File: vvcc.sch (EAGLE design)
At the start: 52 parts, among them IC1 MCP40D19T-5K, IC2 RP2040, IC3 NCP1117LPST33T3G, IC4 16MB_Flash, IC5 LD117ADT-TR, IC6 CLXC8T245QRHLRQ1, J1 Micro-B, J2 302-S301, J3 302-S301, Q1 12MHz

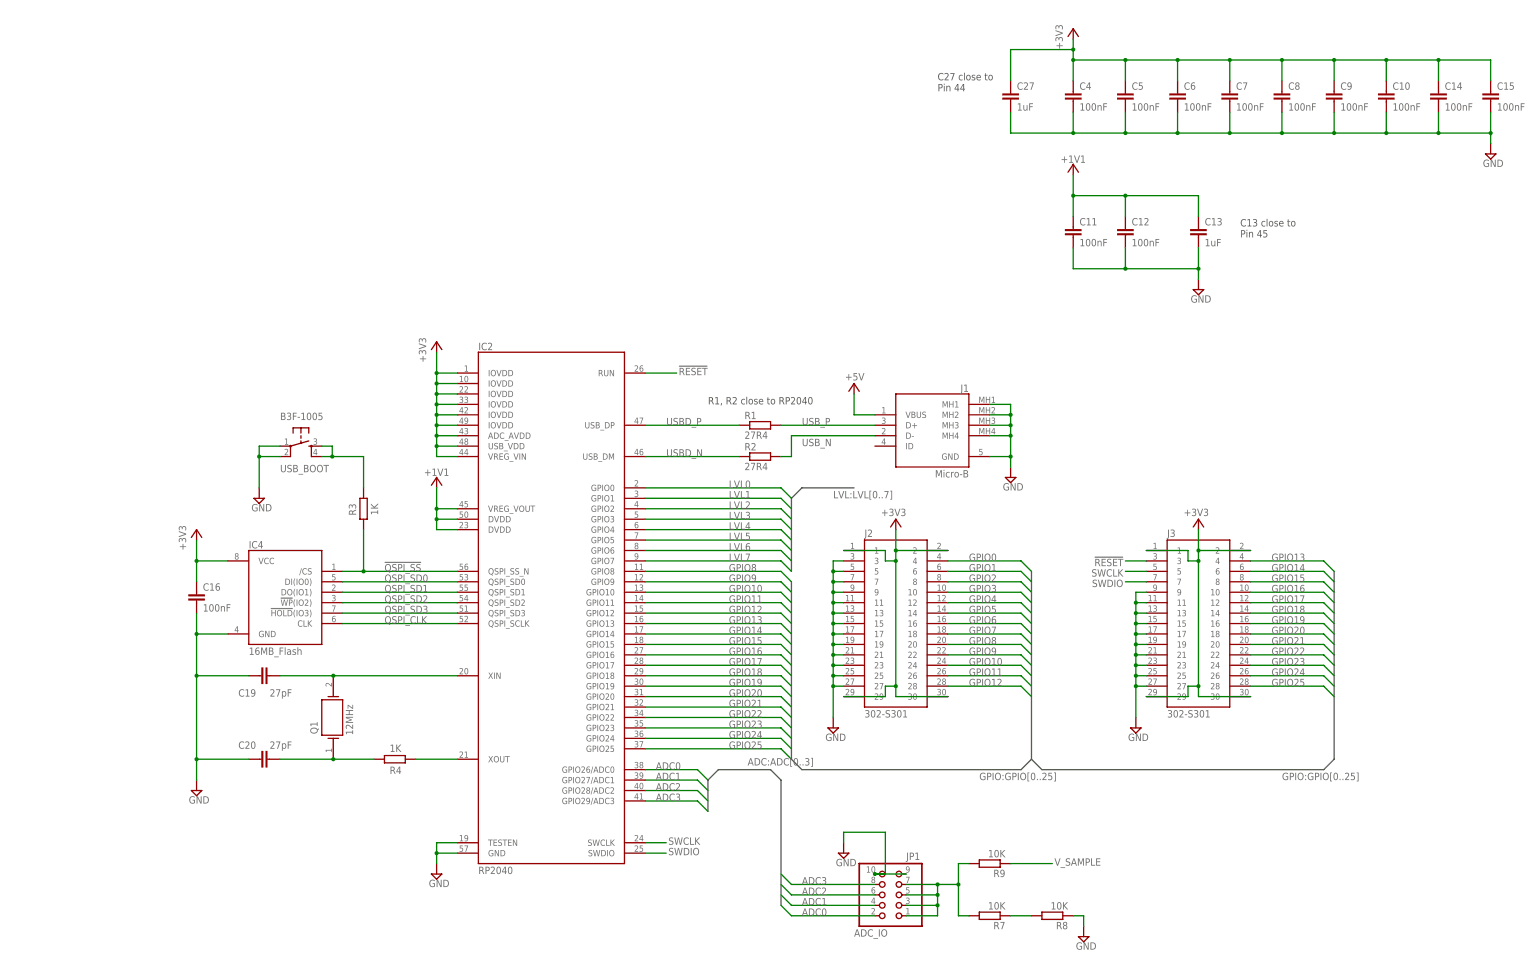
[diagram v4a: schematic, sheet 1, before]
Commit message: Better board layout - and added LEDs. This was the real submit to nextpcb
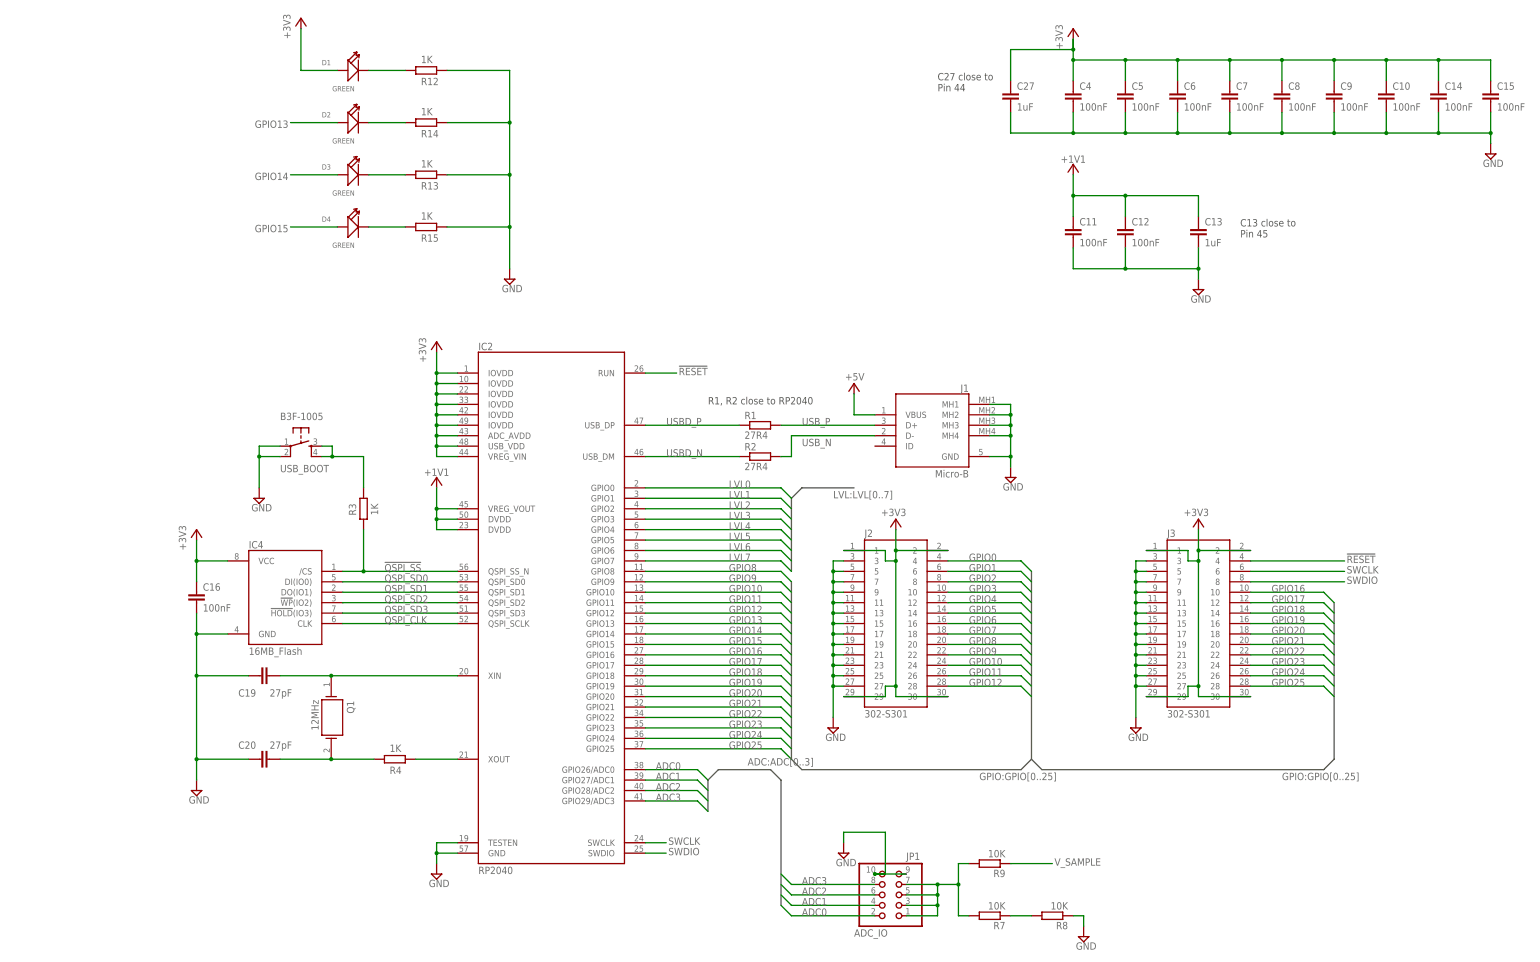
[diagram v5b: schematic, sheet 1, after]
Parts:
- removed C18: 100nF, rcl:C-EUC0201
- removed SPV: MIC803-30D3VM3-TR, x-pi:MIC803-30D2VM3-TR
- added D1, D2, D3, D4: GREEN, Seeed-LED:SMD-LED-CLEAR-BLUE(0603)
- added R12, R13, R14, R15: 1K, rcl:R-EU_R0201
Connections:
- new net N$1: C19.1, IC2.XIN, Q1.1
- new net N$2: C20.2, Q1.2, R4.1
- new net N$3: D1.-, R12.1
- new net N$4: D2.-, R14.1
- net !RESET!: now also J3.4; no longer J3.3, SPV.!RESET!@2
- net +3V3: now also D1.+; no longer C18.1, SPV.VCC@3
- net GND: now also J3.3, J3.5, J3.7, R12.2, R13.2, R14.2, R15.2; no longer C18.2, SPV.GND@1
- net GPIO13: now also D2.+; no longer J3.4
- net GPIO14: now also D3.+; no longer J3.6
- net GPIO15: now also D4.+; no longer J3.8
- net N$6: now also D3.-, R13.1; no longer C19.1, IC2.XIN, Q1.2
- net N$8: now also D4.-, R15.1; no longer C20.2, Q1.1, R4.1
- net SWCLK: now also J3.6; no longer J3.5
- net SWDIO: now also J3.8; no longer J3.7
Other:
- moved on the sheet: Q1, R10
